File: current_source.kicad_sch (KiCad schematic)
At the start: 3 parts, among them Q4 NMOS

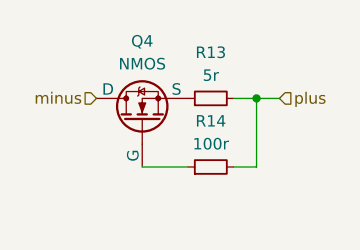
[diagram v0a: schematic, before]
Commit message: Current design with SMD MOSFET (before switching to THT)
🤖 Generated with [Claude Code](https://claude.ai/code)

Co-Authored-By: Claude <noreply@anthropic.com>
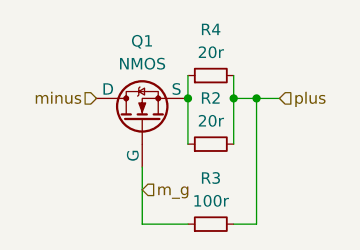
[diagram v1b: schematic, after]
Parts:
- added R4: 20r, Resistor_SMD:R_0805_2012Metric, symbol Device:R_Small
- Q1: renamed from Q4; footprint Package_TO_SOT_THT:TO-220-3_Horizontal_TabDown -> Package_TO_SOT_SMD:SOT-89-3
- R2: renamed from R13; value 5r -> 20r; footprint Resistor_SMD:R_1206_3216Metric -> Resistor_SMD:R_0805_2012Metric
- R3: renamed from R14; footprint Resistor_SMD:R_1206_3216Metric -> Resistor_SMD:R_0805_2012Metric
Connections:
- net plus: now also R4.2
- net m_g: now reaches Q1.2 (G), R3.1
- net at Q1.3 (S), R2.1: now also R4.1
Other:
- moved on the sheet: R2, R3
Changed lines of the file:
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@@
 (kicad_sch
-	(version 20231120)
+	(version 20250114)
 	(generator "eeschema")
-	(generator_version "8.0")
+	(generator_version "9.0")
 	(paper "A4")
 	(junction
@@
 		(color 0 0 0 0)
 	)
+	(junction
+		(at 138.43 97.79)
+		(diameter 0)
+		(color 0 0 0 0)
+	)
+	(junction
+		(at 143.51 97.79)
+		(diameter 0)
+		(color 0 0 0 0)
+	)
 	(wire
 		(pts
@@
 	(wire
 		(pts
-			(xy 146.05 105.41) (xy 146.05 97.79)
-		)
-		(stroke
-			(width 0)
-			(type default)
-		)
-	)
-	(wire
-		(pts
-			(xy 143.51 105.41) (xy 146.05 105.41)
+			(xy 146.05 111.76) (xy 146.05 97.79)
+		)
+		(stroke
+			(width 0)
+			(type default)
+		)
+	)
+	(wire
+		(pts
+			(xy 133.35 111.76) (xy 133.35 105.41)
+		)
+		(stroke
+			(width 0)
+			(type default)
+		)
+	)
+	(wire
+		(pts
+			(xy 138.43 95.25) (xy 138.43 97.79)
+		)
+		(stroke
+			(width 0)
+			(type default)
+		)
+	)
+	(wire
+		(pts
+			(xy 143.51 111.76) (xy 146.05 111.76)
 		)
 		(stroke
@@
 	(wire
 		(pts
-			(xy 133.35 105.41) (xy 138.43 105.41)
+			(xy 133.35 111.76) (xy 138.43 111.76)
+		)
+		(stroke
+			(width 0)
+			(type default)
+		)
+	)
+	(wire
+		(pts
+			(xy 143.51 102.87) (xy 143.51 97.79)
+		)
+		(stroke
+			(width 0)
+			(type default)
+		)
+	)
+	(wire
+		(pts
+			(xy 143.51 95.25) (xy 143.51 97.79)
+		)
+		(stroke
+			(width 0)
+			(type default)
+		)
+	)
+	(wire
+		(pts
+			(xy 138.43 102.87) (xy 138.43 97.79)
 		)
 		(stroke
@@
 		(shape input)
 		(at 128.27 97.79 180)
-		(fields_autoplaced yes)
 		(effects
 			(font
@@
 		)
 	)
+	(hierarchical_label "m_g"
+		(shape input)
+		(at 133.35 107.95 0)
+		(effects
+			(font
+				(size 1.27 1.27)
+			)
+			(justify left)
+		)
+	)
 	(hierarchical_label "plus"
 		(shape input)
 		(at 148.59 97.79 0)
-		(fields_autoplaced yes)
 		(effects
 			(font
@@
 		(dnp no)
 		(fields_autoplaced yes)
-		(property "Reference" "Q4"
+		(property "Reference" "Q1"
 			(at 133.35 91.44 90)
 			(effects
@@
 			)
 		)
-		(property "Footprint" "Package_TO_SOT_THT:TO-220-3_Horizontal_TabDown"
+		(property "Footprint" "Package_TO_SOT_SMD:SOT-89-3"
 			(at 130.81 95.25 0)
 			(effects
@@
 	(symbol
 		(lib_id "Device:R_Small")
-		(at 140.97 105.41 90)
+		(at 140.97 95.25 90)
 		(unit 1)
 		(exclude_from_sim no)
@@
 		(dnp no)
 		(fields_autoplaced yes)
-		(property "Reference" "R14"
-			(at 140.97 100.33 90)
-			(effects
-				(font
-					(size 1.27 1.27)
-				)
-			)
-		)
-		(property "Value" "100r"
-			(at 140.97 102.87 90)
-			(effects
-				(font
-					(size 1.27 1.27)
-				)
-			)
-		)
-		(property "Footprint" "Resistor_SMD:R_1206_3216Metric"
-			(at 140.97 105.41 0)
+		(property "Reference" "R4"
+			(at 140.97 90.17 90)
+			(effects
+				(font
+					(size 1.27 1.27)
+				)
+			)
+		)
+		(property "Value" "20r"
+			(at 140.97 92.71 90)
+			(effects
+				(font
+					(size 1.27 1.27)
+				)
+			)
+		)
+		(property "Footprint" "Resistor_SMD:R_0805_2012Metric"
+			(at 140.97 95.25 0)
 			(effects
 				(font
@@
 		)
 		(property "Datasheet" "~"
-			(at 140.97 105.41 0)
+			(at 140.97 95.25 0)
 			(effects
 				(font
@@
 		)
 		(property "Description" "Resistor, small symbol"
-			(at 140.97 105.41 0)
+			(at 140.97 95.25 0)
 			(effects
 				(font
@@
 			(project "walt-j-shunt"
 				(path "/c8b32050-fabe-49d4-b213-dd23b367e349/6786b1de-24b3-41c2-ac13-9174f173ccc1"
-					(reference "R14")
+					(reference "R5")
 					(unit 1)
 				)
 				(path "/c8b32050-fabe-49d4-b213-dd23b367e349/bcc0eb4b-ef74-4b84-b6d5-2b5ad0313de0"
-					(reference "R3")
+					(reference "R4")
 					(unit 1)
 				)
@@
 	(symbol
 		(lib_id "Device:R_Small")
-		(at 140.97 97.79 90)
+		(at 140.97 111.76 90)
 		(unit 1)
 		(exclude_from_sim no)
@@
 		(dnp no)
 		(fields_autoplaced yes)
-		(property "Reference" "R13"
-			(at 140.97 92.71 90)
-			(effects
-				(font
-					(size 1.27 1.27)
-				)
-			)
-		)
-		(property "Value" "5r"
-			(at 140.97 95.25 90)
-			(effects
-				(font
-					(size 1.27 1.27)
-				)
-			)
-		)
-		(property "Footprint" "Resistor_SMD:R_1206_3216Metric"
-			(at 140.97 97.79 0)
+		(property "Reference" "R3"
+			(at 140.97 106.68 90)
+			(effects
+				(font
+					(size 1.27 1.27)
+				)
+			)
+		)
+		(property "Value" "100r"
+			(at 140.97 109.22 90)
+			(effects
+				(font
+					(size 1.27 1.27)
+				)
+			)
+		)
+		(property "Footprint" "Resistor_SMD:R_0805_2012Metric"
+			(at 140.97 111.76 0)
 			(effects
 				(font
@@
 		)
 		(property "Datasheet" "~"
-			(at 140.97 97.79 0)
+			(at 140.97 111.76 0)
 			(effects
 				(font
@@
 		)
 		(property "Description" "Resistor, small symbol"
-			(at 140.97 97.79 0)
-			(effects
-				(font
+			(at 140.97 111.76 0)
+			(effects
+				(font
+					(size 1.27 1.27)
+				)
+				(hide yes)
+			)
+		)
+		(pin "2"
+		)
+		(pin "1"
+		)
+		(instances
+			(project "walt-j-shunt"
+				(path "/c8b32050-fabe-49d4-b213-dd23b367e349/6786b1de-24b3-41c2-ac13-9174f173ccc1"
+					(reference "R14")
+					(unit 1)
+				)
+				(path "/c8b32050-fabe-49d4-b213-dd23b367e349/bcc0eb4b-ef74-4b84-b6d5-2b5ad0313de0"
+					(reference "R3")
+					(unit 1)
+				)
+			)
+		)
+	)
+	(symbol
+		(lib_id "Device:R_Small")
+		(at 140.97 102.87 90)
+		(unit 1)
+		(exclude_from_sim no)
+		(in_bom yes)
+		(on_board yes)
+		(dnp no)
+		(property "Reference" "R2"
+			(at 140.97 97.79 90)
+			(effects
+				(font
+					(size 1.27 1.27)
+				)
+			)
+		)
+		(property "Value" "20r"
+			(at 140.97 100.33 90)
+			(effects
+				(font
+					(size 1.27 1.27)
+				)
+			)
+		)
+		(property "Footprint" "Resistor_SMD:R_0805_2012Metric"
+			(at 140.97 102.87 0)
+			(effects
+				(font
+					(size 1.27 1.27)
+				)
+				(hide yes)
+			)
+		)
+		(property "Datasheet" "~"
+			(at 140.97 102.87 0)
+			(effects
+				(font
+					(size 1.27 1.27)
+				)
+				(hide yes)
+			)
+		)
+		(property "Description" "Resistor, small symbol"
+			(at 140.97 102.87 0)
+			(effects
+				(font

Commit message: Switch to THT MOSFET - need to verify pinout, rough but closer
🤖 Generated with [Claude Code](https://claude.ai/code)

Co-Authored-By: Claude <noreply@anthropic.com>
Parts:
- Q1: footprint Package_TO_SOT_SMD:SOT-89-3 -> Package_TO_SOT_THT:TO-92_Inline
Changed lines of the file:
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@@
 			)
 		)
-		(property "Footprint" "Package_TO_SOT_SMD:SOT-89-3"
+		(property "Footprint" "Package_TO_SOT_THT:TO-92_Inline"
 			(at 130.81 95.25 0)
 			(effects
